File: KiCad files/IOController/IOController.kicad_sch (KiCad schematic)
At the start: 13 parts, among them J1 AVR-ISP-6, J2 XT60 Horizontal Male, J3 XT60 Horizontal Socket, J4 Conn_01x02, J5 Conn_01x02, SW1 RotaryEncoder_Switch, SW2 SW_Push, U1 ATtiny85-20P, U3 LP2985-1.8

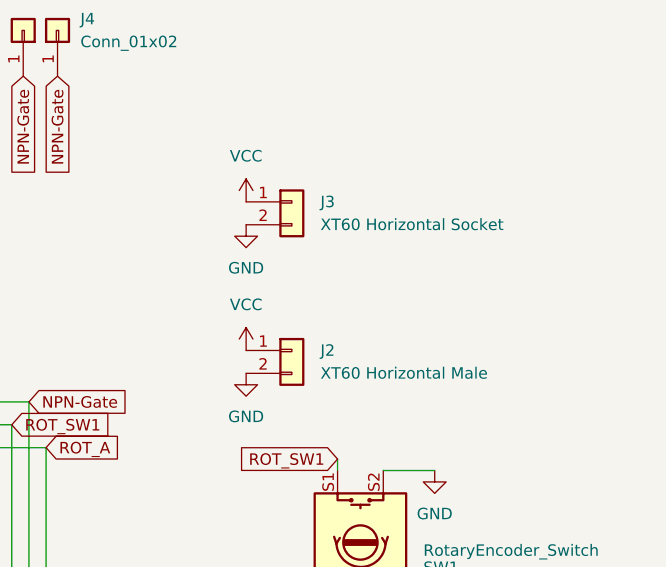
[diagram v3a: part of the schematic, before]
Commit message: corrected VCC and GND being swapped
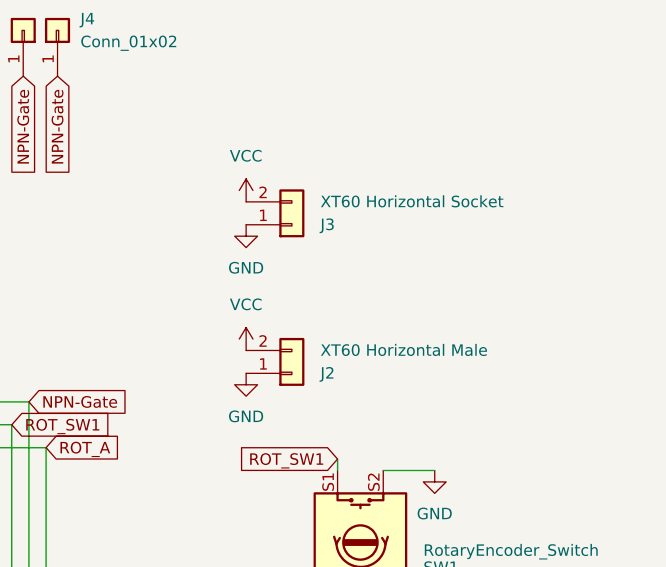
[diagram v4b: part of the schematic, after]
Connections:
- net GND: now also J2.1 (Pin_1), J3.1 (Pin_1); no longer J2.2 (Pin_2), J3.2 (Pin_2)
- net VCC: now also J2.2 (Pin_2), J3.2 (Pin_2); no longer J2.1 (Pin_1), J3.1 (Pin_1)
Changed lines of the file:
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@@
     )
   )
-  (symbol (lib_id "Connector_Generic:Conn_01x02") (at 109.855 58.42 0) (unit 1)
-    (in_bom yes) (on_board yes) (dnp no) (fields_autoplaced)
-    (property "Reference" "J2" (at 113.03 58.42 0)
+  (symbol (lib_id "Connector_Generic:Conn_01x02") (at 109.855 60.96 0) (mirror x) (unit 1)
+    (in_bom yes) (on_board yes) (dnp no)
+    (property "Reference" "J2" (at 113.03 60.96 0)
       (effects (font (size 1.27 1.27)) (justify left))
     )
-    (property "Value" "XT60 Horizontal Male" (at 113.03 60.96 0)
+    (property "Value" "XT60 Horizontal Male" (at 113.03 58.42 0)
       (effects (font (size 1.27 1.27)) (justify left))
     )
-    (property "Footprint" "Connector_AMASS:AMASS_XT60PW-M_1x02_P7.20mm_Horizontal" (at 109.855 58.42 0)
+    (property "Footprint" "Connector_AMASS:AMASS_XT60PW-M_1x02_P7.20mm_Horizontal" (at 109.855 60.96 0)
       (effects (font (size 1.27 1.27)) hide)
     )
-    (property "Datasheet" "~" (at 109.855 58.42 0)
+    (property "Datasheet" "~" (at 109.855 60.96 0)
       (effects (font (size 1.27 1.27)) hide)
     )
@@
     )
   )
-  (symbol (lib_id "Connector_Generic:Conn_01x02") (at 109.855 41.91 0) (unit 1)
-    (in_bom yes) (on_board yes) (dnp no) (fields_autoplaced)
-    (property "Reference" "J3" (at 113.03 41.91 0)
+  (symbol (lib_id "Connector_Generic:Conn_01x02") (at 109.855 44.45 0) (mirror x) (unit 1)
+    (in_bom yes) (on_board yes) (dnp no)
+    (property "Reference" "J3" (at 113.03 44.45 0)
       (effects (font (size 1.27 1.27)) (justify left))
     )
-    (property "Value" "XT60 Horizontal Socket" (at 113.03 44.45 0)
+    (property "Value" "XT60 Horizontal Socket" (at 113.03 41.91 0)
       (effects (font (size 1.27 1.27)) (justify left))
     )
-    (property "Footprint" "Connector_AMASS:AMASS_XT60PW-F_1x02_P7.20mm_Horizontal" (at 109.855 41.91 0)
+    (property "Footprint" "Connector_AMASS:AMASS_XT60PW-F_1x02_P7.20mm_Horizontal" (at 109.855 44.45 0)
       (effects (font (size 1.27 1.27)) hide)
     )
-    (property "Datasheet" "~" (at 109.855 41.91 0)
+    (property "Datasheet" "~" (at 109.855 44.45 0)
       (effects (font (size 1.27 1.27)) hide)
     )

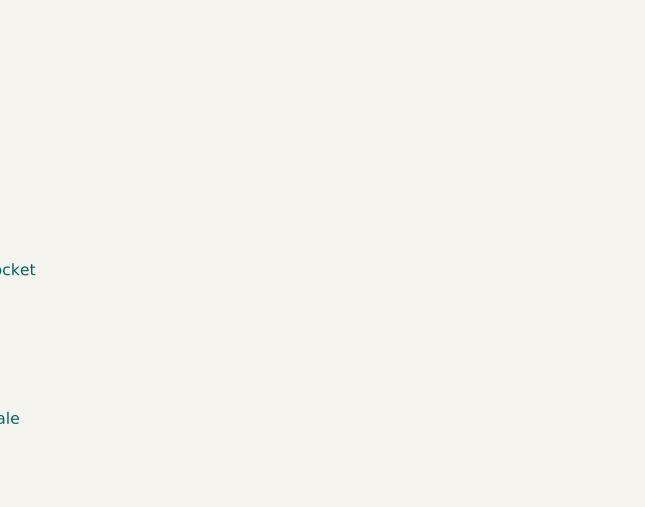
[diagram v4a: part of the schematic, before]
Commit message: changed an XT60 to edge connector because I didnt like the XT60 and pin header setup.
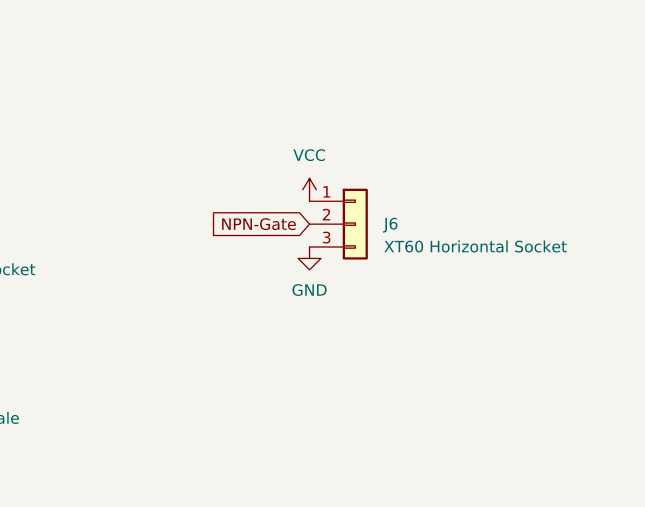
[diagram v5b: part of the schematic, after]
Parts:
- added J6: XT60 Horizontal Socket, Connector_PinHeader_2.54mm:PinHeader_1x03_P2.54mm_Vertical, symbol Connector_Generic:Conn_01x03
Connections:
- net GND: now also J6.3 (Pin_3)
- net NPN-Gate: now also J6.2 (Pin_2)
- net VCC: now also J6.1 (Pin_1)
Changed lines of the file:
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@@
+    )
+  )
+  (global_label "NPN-Gate" (shape input) (at 163.83 36.83 180) (fields_autoplaced)
+    (effects (font (size 1.27 1.27)) (justify right))
+    (property "Intersheetrefs" "${INTERSHEET_REFS}" (at 151.1081 36.83 0)
+      (effects (font (size 1.27 1.27)) (justify right) hide)
     )
   )
@@
     )
   )
+  (symbol (lib_id "power:GND") (at 163.83 39.37 0) (unit 1)
+    (in_bom yes) (on_board yes) (dnp no) (fields_autoplaced)
+    (property "Reference" "#PWR016" (at 163.83 45.72 0)
+      (effects (font (size 1.27 1.27)) hide)
+    )
+    (property "Value" "GND" (at 163.83 44.196 0)
+      (effects (font (size 1.27 1.27)))
+    )
+    (property "Footprint" "" (at 163.83 39.37 0)
+      (effects (font (size 1.27 1.27)) hide)
+    )
+    (property "Datasheet" "" (at 163.83 39.37 0)
+      (effects (font (size 1.27 1.27)) hide)
+    )
+    (pin "1")
+    (instances
+      (project "IOController"
+        (path "/f1c719f6-f1ad-4e81-8891-bde8a483290d"
+          (reference "#PWR016") (unit 1)
+        )
+      )
+    )
+  )
   (symbol (lib_id "Device:C_Small") (at 54.61 27.94 0) (unit 1)
     (in_bom yes) (on_board yes) (dnp no)
@@
         )
       )
+    )
+  )
+  (symbol (lib_id "Connector_Generic:Conn_01x03") (at 168.91 36.83 0) (unit 1)
+    (in_bom yes) (on_board yes) (dnp no)
+    (property "Reference" "J6" (at 172.085 36.83 0)
+      (effects (font (size 1.27 1.27)) (justify left))
+    )
+    (property "Value" "XT60 Horizontal Socket" (at 172.085 39.37 0)
+      (effects (font (size 1.27 1.27)) (justify left))
+    )
+    (property "Footprint" "Connector_PinHeader_2.54mm:PinHeader_1x03_P2.54mm_Vertical" (at 168.91 36.83 0)
+      (effects (font (size 1.27 1.27)) hide)
+    )
+    (property "Datasheet" "~" (at 168.91 36.83 0)
+      (effects (font (size 1.27 1.27)) hide)
+    )
+    (pin "1")
+    (pin "2")
+    (pin "3")
+    (instances
+      (project "IOController"
+        (path "/f1c719f6-f1ad-4e81-8891-bde8a483290d"
+          (reference "J6") (unit 1)
+        )
+      )
+    )
+  )
+  (symbol (lib_id "power:VCC") (at 163.83 34.29 0) (unit 1)
+    (in_bom yes) (on_board yes) (dnp no) (fields_autoplaced)
+    (property "Reference" "#PWR015" (at 163.83 38.1 0)
+      (effects (font (size 1.27 1.27)) hide)
+    )
+    (property "Value" "VCC" (at 163.83 29.21 0)
+      (effects (font (size 1.27 1.27)))
+    )
+    (property "Footprint" "" (at 163.83 34.29 0)
+      (effects (font (size 1.27 1.27)) hide)
+    )
+    (property "Datasheet" "" (at 163.83 34.29 0)
+      (effects (font (size 1.27 1.27)) hide)
+    )
+    (pin "1")
+    (instances
+      (project "IOController"
+        (path "/f1c719f6-f1ad-4e81-8891-bde8a483290d"
+          (reference "#PWR015") (unit 1)
+        )
+      )

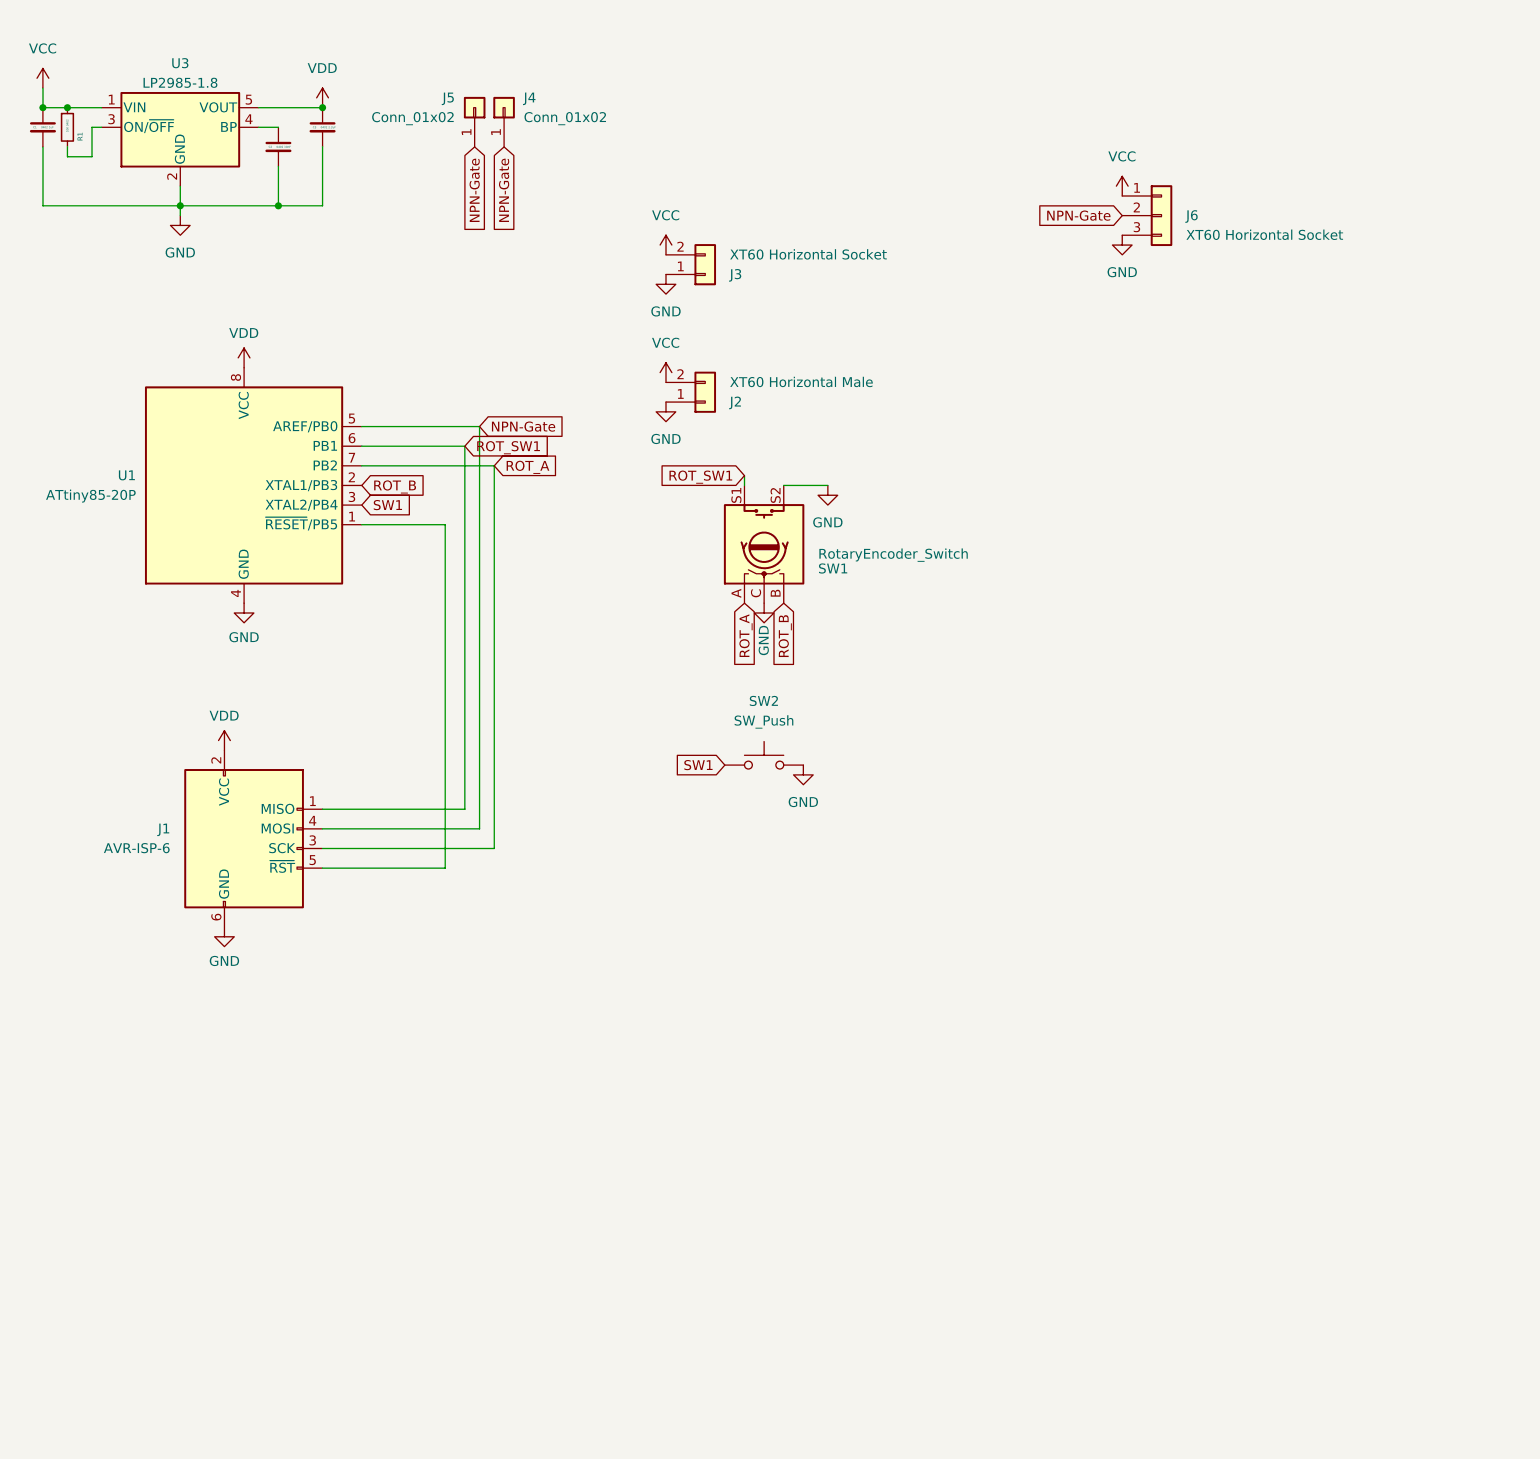
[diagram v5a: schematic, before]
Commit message: added footprints for some discontinued LEDs i have spare of, added level shifter to ensure gate voltage is above threshold
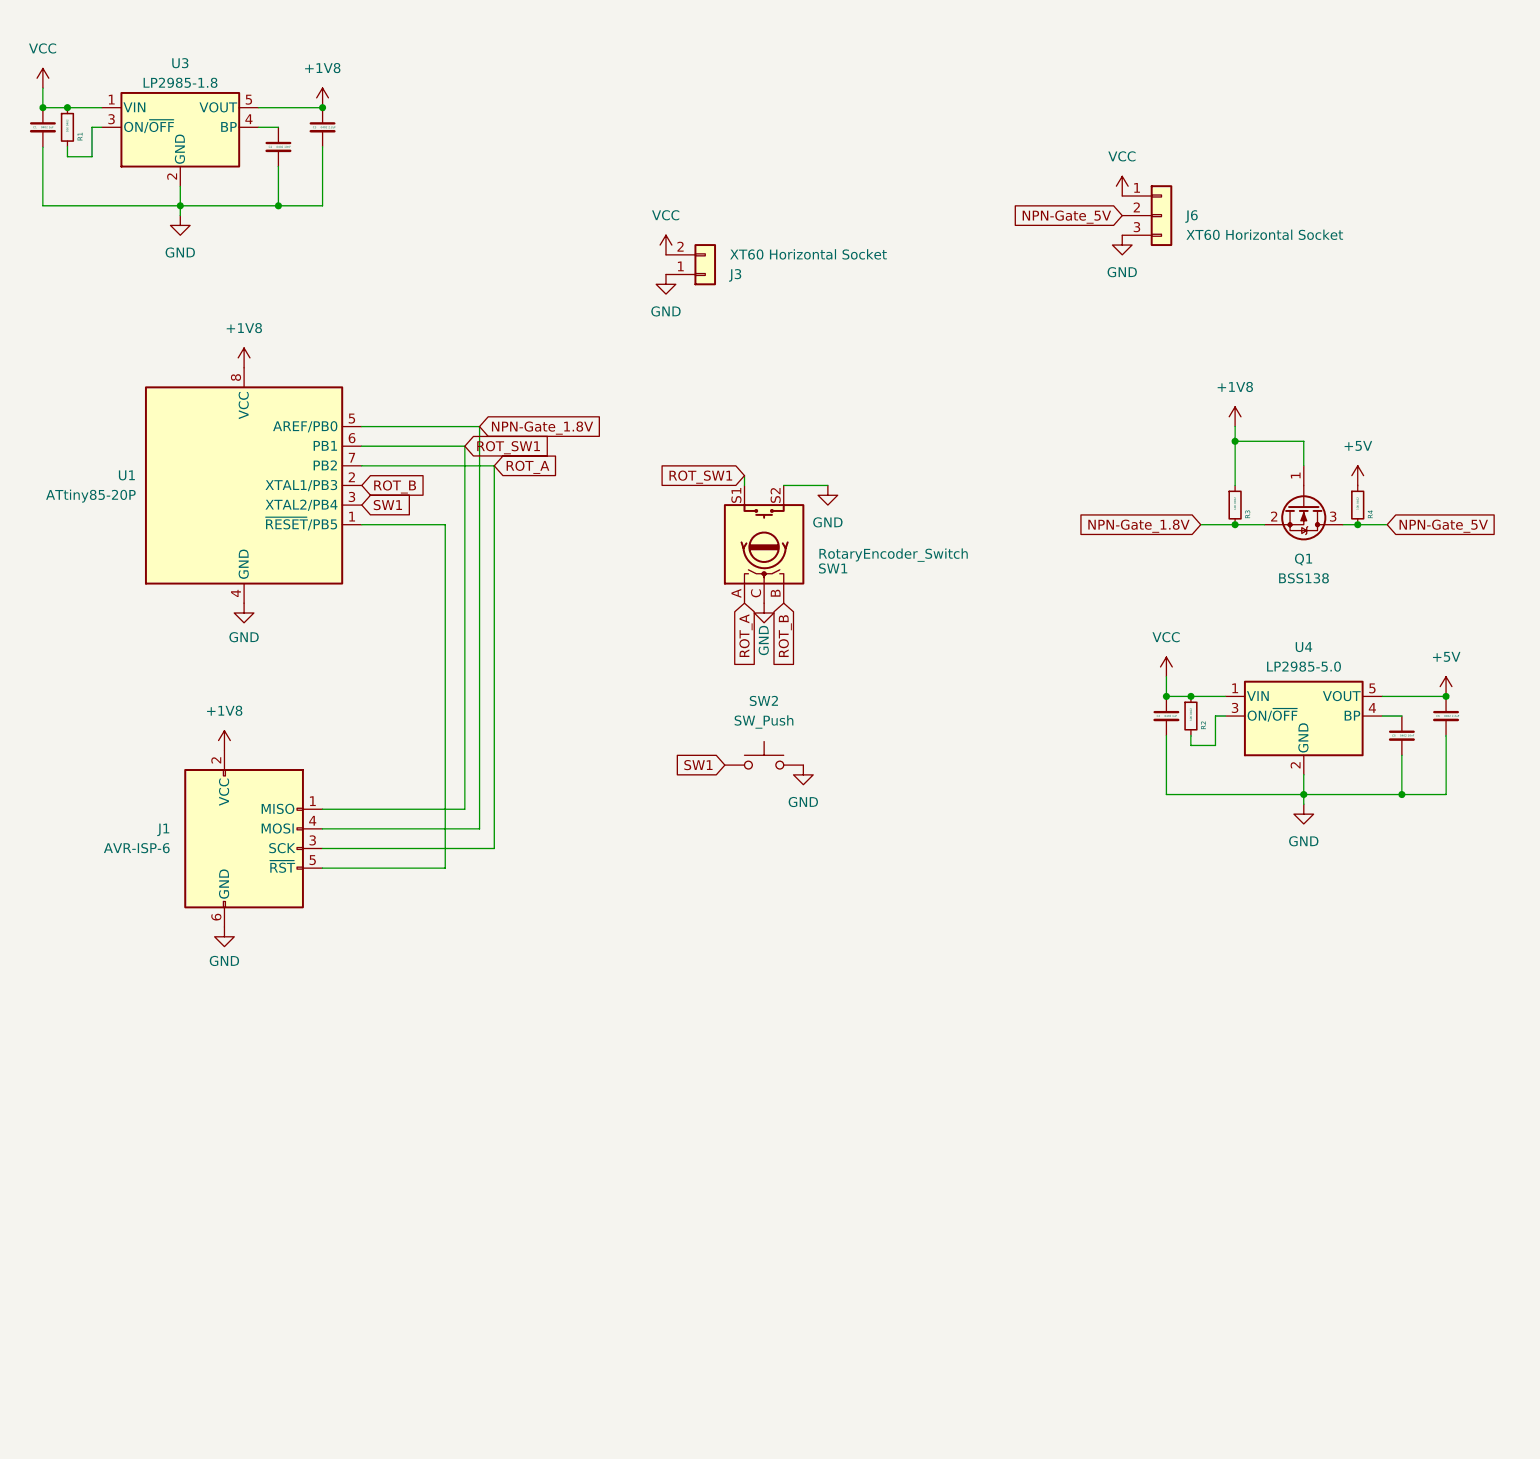
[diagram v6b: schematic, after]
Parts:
- removed J2: XT60 Horizontal Male, Connector_AMASS:AMASS_XT60PW-M_1x02_P7.20mm_Horizontal, symbol Connector_Generic:Conn_01x02
- removed J4, J5: Conn_01x02, Connector_PinHeader_2.54mm:PinHeader_1x01_P2.54mm_Horizontal, symbol Connector_Generic:Conn_01x01
- added C4: 0402 1uF, Capacitor_SMD:C_0402_1005Metric, symbol Device:C_Small
- added C5: 0402 10nF, Capacitor_SMD:C_0402_1005Metric, symbol Device:C_Small
- added C6: 0402 2.2uF, Capacitor_SMD:C_0402_1005Metric, symbol Device:C_Small
- added Q1: BSS138, Package_TO_SOT_SMD:SOT-23, symbol Transistor_FET:BSS138
- added R2, R3, R4: 10K 0402, Resistor_SMD:R_0402_1005Metric, symbol Device:R_Small
- added U4: LP2985-5.0, Package_TO_SOT_SMD:SOT-23-5, symbol Regulator_Linear:LP2985-1.8
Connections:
- net GND: now also C4.2, C5.2, C6.2, U4.2 (GND)
- net VCC: now also C4.1, R2.1, U4.1 (VIN)
- net NPN-Gate renamed NPN-Gate_1.8V
- net NPN-Gate_1.8V: now also Q1.2 (S), R3.2; no longer J6.2 (Pin_2)
- net VDD renamed +1V8
- net +1V8: now also Q1.1 (G), R3.1
- new net: C5.1, U4.4 (BP)
- new net: R2.2, U4.3 (ON/~{OFF})
- new net +5V: C6.1, R4.1, U4.5 (VOUT)
- new net NPN-Gate_5V: J6.2 (Pin_2), Q1.3 (D), R4.2

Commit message: some partial work towards modifying the design yet again
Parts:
- added C10: 22uF, Capacitor_SMD:C_0805_2012Metric, symbol Device:C_Small
- added C11, C9: 100nF, Capacitor_SMD:C_0805_2012Metric, symbol Device:C_Small
- added C7: 10uF 0805, Capacitor_SMD:C_0805_2012Metric, symbol Device:C_Small
- added C8: 100nF 0805, Capacitor_SMD:C_0805_2012Metric, symbol Device:C_Small
- added L1: MDA7030-2R2M, Inductor_SMD:L_Coilcraft_XAL7030-222, symbol Device:L
- added PS1: TPS566242DRLR, Package_TO_SOT_SMD:SOT-563, symbol TPS566242DRLR:TPS566242DRLR
- added R5: 100K 0805, Resistor_SMD:R_0805_2012Metric, symbol Device:R_Small
- added R6: 23.2K 0805, Resistor_SMD:R_0805_2012Metric, symbol Device:R_Small
- added R7: 120K 0805, Resistor_SMD:R_0805_2012Metric, symbol Device:R_Small
- added R8: 30K 0805, Resistor_SMD:R_0805_2012Metric, symbol Device:R_Small
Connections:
- net GND: now also C10.2, C11.2, C7.2, C8.2, PS1.3 (GND), PS1.4 (AGND), R6.2, R8.2
- net NPN-Gate_5V: no longer J6.2 (Pin_2)
- net VCC: now also C7.1, C8.1, PS1.1 (VIN), R5.2; no longer J6.1 (Pin_1)
- new net: C9.2, PS1.6 (FB), R7.2, R8.1
- new net: PS1.5 (EN), R5.1, R6.1
- new net: L1.1, PS1.2 (SW)
- new net VDD: C10.1, C11.1, C9.1, J6.1 (Pin_1), L1.2, R7.1
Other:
- note added: "Inductor should be: 2.2uH 13.6mOhm"
- note added: "mebe swap for reed switch for waterproof ver"

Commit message: changed regulator again
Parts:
- removed C10: 22uF, Capacitor_SMD:C_0805_2012Metric, symbol Device:C_Small
- removed C11, C9: 100nF, Capacitor_SMD:C_0805_2012Metric, symbol Device:C_Small
- removed C7: 10uF 0805, Capacitor_SMD:C_0805_2012Metric, symbol Device:C_Small
- removed C8: 100nF 0805, Capacitor_SMD:C_0805_2012Metric, symbol Device:C_Small
- removed L1: MDA7030-2R2M, Inductor_SMD:L_Coilcraft_XAL7030-222, symbol Device:L
- removed PS1: TPS566242DRLR, Package_TO_SOT_SMD:SOT-563, symbol TPS566242DRLR:TPS566242DRLR
- removed R5: 100K 0805, Resistor_SMD:R_0805_2012Metric, symbol Device:R_Small
- removed R6: 23.2K 0805, Resistor_SMD:R_0805_2012Metric, symbol Device:R_Small
- removed R7: 120K 0805, Resistor_SMD:R_0805_2012Metric, symbol Device:R_Small
- removed R8: 30K 0805, Resistor_SMD:R_0805_2012Metric, symbol Device:R_Small
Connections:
- net GND: no longer J6.3 (Pin_3)
- net NPN-Gate_1.8V renamed LED_PWM_1V8
- net NPN-Gate_5V renamed LED_PWM_5V
- net VDD renamed LED_V+
- new net LED_V-: J6.3 (Pin_3)
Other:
- added sheet LED Driver (LedDriver.kicad_sch)
- note removed: "Inductor should be: 2.2uH 13.6mOhm"
- note removed: "mebe swap for reed switch for waterproof ver"
